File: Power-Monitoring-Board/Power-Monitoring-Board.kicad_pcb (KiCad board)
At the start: 2 copper layers, 127 x 72 mm, 47 parts, among them IC1 XC6222D331MR-G, J1 Conn_01x02_Pin, J2 Conn_01x02_Pin, J3 Conn_01x01_Pin, J4 Conn_01x01_Pin, J5 Conn_01x01_Pin, J6 Conn_01x01_Pin, J7 Conn_01x02_Pin, J8 Conn_01x02_Pin, SW1 GF-123-0054, U1 INA260AIPWR, U2 CR2450, U3 MAX17043G+U, U4 NUCLEO_L432KC, U5 ST7735R

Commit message: more changes
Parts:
- moved D2 11.9 mm to (152.8, 69.4)
- moved R2 11.9 mm to (152.8, 71.2)
- moved R13 8.07 mm to (127.6, 115.0)
- moved D1 6.15 mm to (159.0, 69.3)
- moved D3 6.15 mm to (165.0, 69.3)
- moved R1 6.15 mm to (159.0, 71.2)
- moved R5 6.15 mm to (165.0, 71.2)
- moved R3 4.50 mm to (139.8, 123.7)
- moved R9 4.42 mm to (118.1, 95.9), turned to -90 degrees
- moved C1 3.70 mm to (106.1, 100.8), turned to -90 degrees
- moved R12 2.97 mm to (142.7, 120.3)
- moved C3 2.95 mm to (138.2, 121.5)
- moved R8 2.83 mm to (130.5, 120.0)
- moved R11 2.66 mm to (144.8, 120.3), turned to -90 degrees
- moved R10 2.36 mm to (120.3, 95.9)
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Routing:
- net /Batt: track 132.2 -> 114.3 mm
- net Net-(D2-K): track 71.2 -> 59.4 mm
- net /ALERT: track 36.5 -> 31.7 mm
- net Net-(U3-CELL): track 11.3 -> 6.76 mm
- net /SCL: track 100.2 -> 103.0 mm
- net Net-(U3-VDD): track 11.8 -> 9.42 mm
- net /V-: track 2.86 -> 1.70 mm
- net /V+: track 9.28 -> 8.13 mm
- net GND: track 13.4 -> 12.8 mm
- net /SDA: track 104.3 -> 104.0 mm, vias 4 -> 2

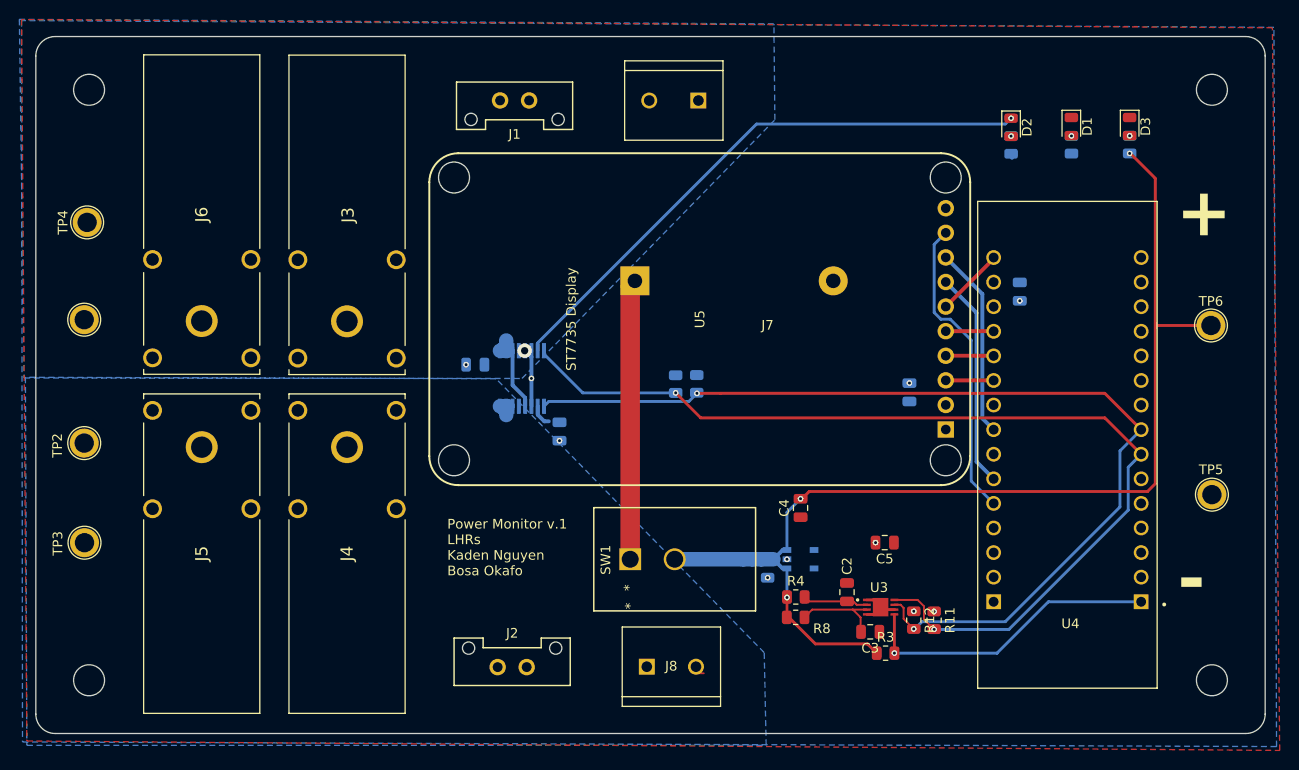
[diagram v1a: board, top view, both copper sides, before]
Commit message: added labels
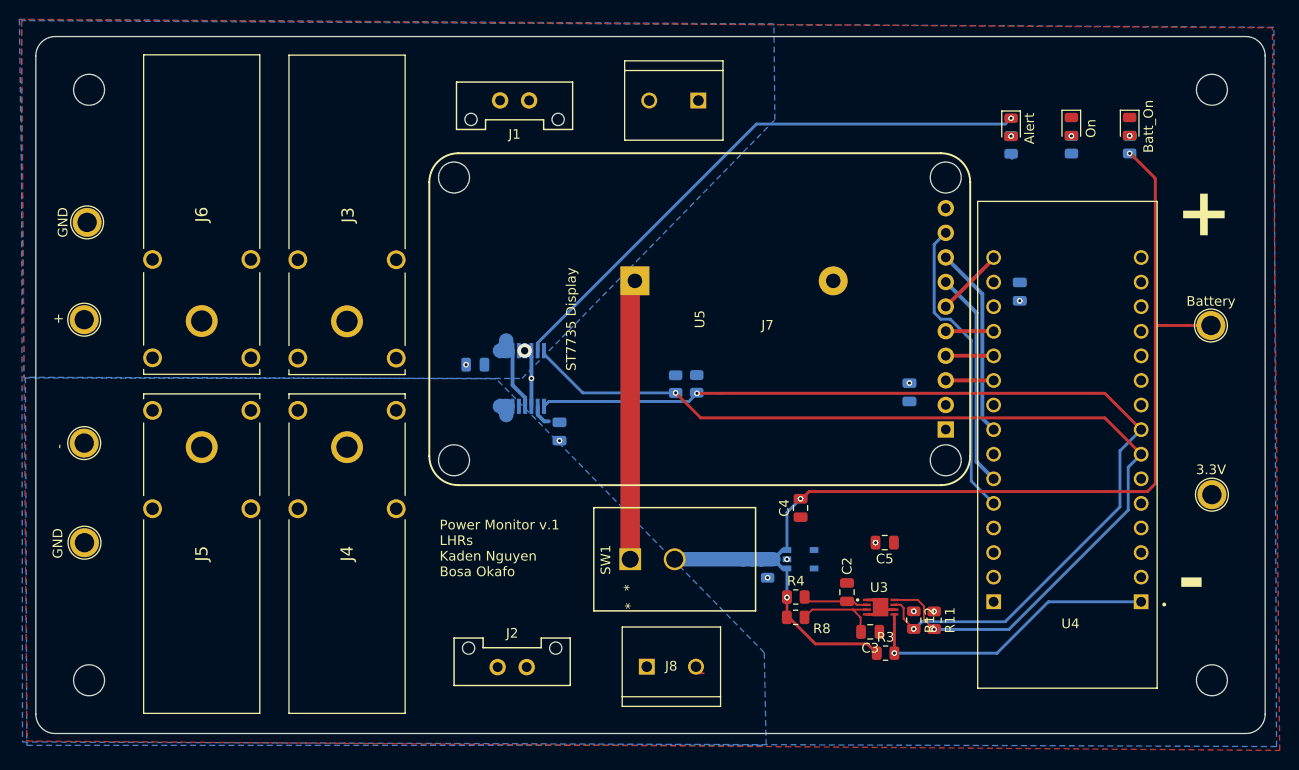
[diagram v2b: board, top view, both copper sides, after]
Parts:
- renumbered TP2 to -, TP5 to 3.3V, D2 to Alert, D3 to Batt_On, TP6 to Battery, TP3 to GND, TP4 to GND, D1 to On
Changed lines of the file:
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@@
 		(descr "Plated Hole as test Point, diameter 2.0mm")
 		(tags "test point plated hole")
-		(property "Reference" "TP3"
+		(property "Reference" "GND"
 			(at -0.07 -2.758 90)
 			(layer "F.SilkS")
@@
 		(descr "Plated Hole as test Point, diameter 2.0mm")
 		(tags "test point plated hole")
-		(property "Reference" "TP2"
+		(property "Reference" "-"
 			(at -0.24 -2.768 90)
 			(layer "F.SilkS")
+			(hide yes)
 			(effects
 				(font
@@
 		(descr "LED SMD 0805 (2012 Metric), square (rectangular) end terminal, IPC_7351 nominal, (Body size source: https://docs.google.com/spreadsheets/d/1BsfQQcO9C6DZCsRaXUlFlo91Tg2WpOkGARC1WS5S8t0/edit?usp=sharing), generated with kicad-footprint-generator")
 		(tags "LED")
-		(property "Reference" "D3"
-			(at 0 -1.65 90)
+		(property "Reference" "Batt_On"
+			(at -0.02 -1.95 90)
 			(layer "F.SilkS")
 			(effects
@@
 		)
 		(property "Value" "Batt_On_LED"
-			(at 0 1.65 90)
+			(at 0.62 2.12 90)
 			(layer "F.Fab")
 			(effects
@@
 		(tags "capacitor")
 		(property "Reference" "C4"
-			(at 0 -1.68 270)
+			(at 0 -1.68 -90)
 			(layer "F.SilkS")
 			(effects
@@
 		)
 		(property "Value" "1uF"
-			(at -36.025 -31.57 270)
+			(at -36.025 -31.57 -90)
 			(layer "B.Fab")
 			(effects
@@
 		)
 		(fp_text user "${REFERENCE}"
-			(at 0 0 270)
+			(at 0 0 -90)
 			(layer "F.Fab")
 			(effects
@@
 		(descr "Plated Hole as test Point, diameter 2.0mm")
 		(tags "test point plated hole")
-		(property "Reference" "TP5"
+		(property "Reference" "3.3V"
 			(at 0.09 2.58 180)
 			(layer "F.SilkS")
@@
 		(descr "Plated Hole as test Point, diameter 2.0mm")
 		(tags "test point plated hole")
-		(property "Reference" "TP4"
+		(property "Reference" "GND"
 			(at 0 -2.498 90)
 			(layer "F.SilkS")
@@
 		(descr "LED SMD 0805 (2012 Metric), square (rectangular) end terminal, IPC_7351 nominal, (Body size source: https://docs.google.com/spreadsheets/d/1BsfQQcO9C6DZCsRaXUlFlo91Tg2WpOkGARC1WS5S8t0/edit?usp=sharing), generated with kicad-footprint-generator")
 		(tags "LED")
-		(property "Reference" "D1"
-			(at 0 -1.65 90)
+		(property "Reference" "On"
+			(at 0.2 -2.025 90)
 			(layer "F.SilkS")
 			(effects
@@
 		(descr "LED SMD 0805 (2012 Metric), square (rectangular) end terminal, IPC_7351 nominal, (Body size source: https://docs.google.com/spreadsheets/d/1BsfQQcO9C6DZCsRaXUlFlo91Tg2WpOkGARC1WS5S8t0/edit?usp=sharing), generated with kicad-footprint-generator")
 		(tags "LED")
-		(property "Reference" "D2"
-			(at 0 -1.65 90)
+		(property "Reference" "Alert"
+			(at 0.125 -1.91 90)
 			(layer "F.SilkS")
 			(effects
@@
 		)
 		(property "Value" "Alert_LED"
-			(at 1.9425 1.64 90)
+			(at 1.615 2.42 90)
 			(layer "B.Fab")
 			(effects
@@
 		(descr "Plated Hole as test Point, diameter 2.0mm")
 		(tags "test point plated hole")
-		(property "Reference" "TP6"
+		(property "Reference" "Battery"
 			(at 0 -2.498 0)
 			(layer "F.SilkS")
@@
 		(fp_arc
 			(start 4.01 -3.6)
-			(mid 3.809264 -3.345931)
+			(mid 3.809264 -3.345927)
 			(end 3.5 -3.25)
 			(stroke
@@
 		(tags "capacitor")
 		(property "Reference" "C8"
-			(at 0 1.68 360)
+			(at 0 1.68 0)
 			(layer "B.SilkS")
 			(effects
@@
 		)
 		(property "Value" "0.1uF"
-			(at 0 -1.68 360)
+			(at 0 -1.68 0)
 			(layer "B.Fab")
 			(effects
@@
 		)
 		(fp_text user "${REFERENCE}"
-			(at 0 0 360)
+			(at 0 0 0)
 			(layer "B.Fab")
 			(effects
@@
 		(tags "resistor")
 		(property "Reference" "R13"
-			(at 0 1.65 270)
+			(at 0 1.65 -90)
 			(layer "B.SilkS")
 			(effects
@@
 		)
 		(property "Value" "10k"
-			(at 0 -1.65 270)
+			(at 0 -1.65 -90)
 			(layer "B.Fab")
 			(effects
@@
 		)
 		(fp_text user "${REFERENCE}"
-			(at 0 0 270)
+			(at 0 0 -90)
 			(layer "B.Fab")
 			(effects
@@
 	)
 	(gr_text "Power Monitor v.1        \nLHRs   \nKaden Nguyen\nBosa Okafo\n                          \n\n"
-		(at 94.5 119 0)
+		(at 93.71 119.09 0)
 		(layer "F.SilkS")
 		(effects
@@
 		)
 	)
+	(gr_text "+\n"
+		(locked yes)
+		(at 54.32 89.15 90)
+		(layer "F.SilkS")
+		(effects
+			(font
+				(size 1 1)
+				(thickness 0.15)
+			)
+		)
+	)
 	(gr_text "-\n"
 		(at 169.96 118.95 0)
@@
 		)
 	)
+	(gr_text "-"
+		(at 54.39 102.35 90)
+		(layer "F.SilkS")
+		(effects
+			(font
+				(size 1 1)
+				(thickness 0.15)
+			)
+		)
+	)

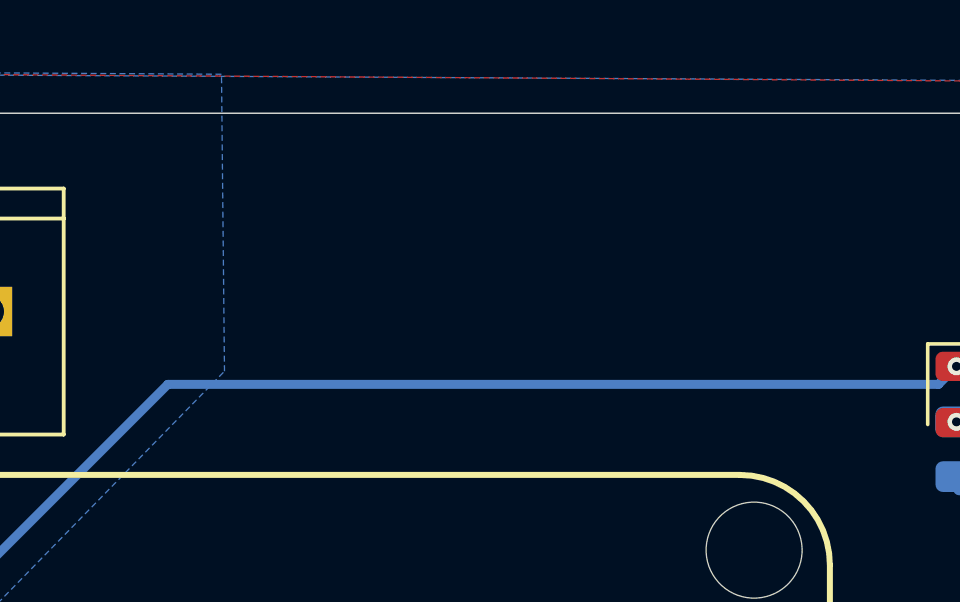
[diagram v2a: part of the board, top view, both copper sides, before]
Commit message: added utsvt logo
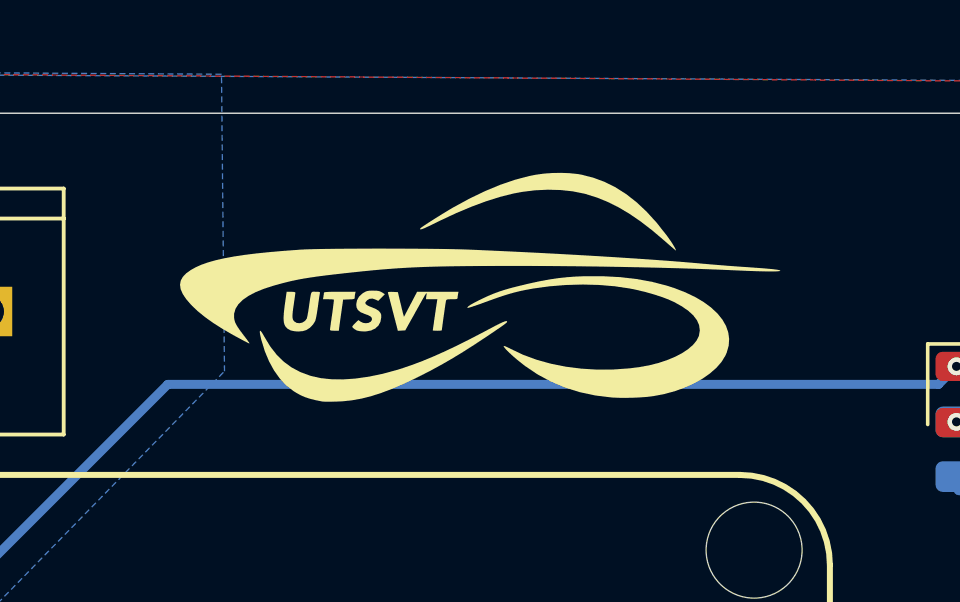
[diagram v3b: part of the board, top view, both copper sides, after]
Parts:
- added G***: LOGO, LOGO, F.Cu at (136.9, 65.8)
